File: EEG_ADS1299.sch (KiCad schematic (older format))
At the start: 76 parts, among them IC1 ADS1299, P1 CONN_2, P2 CONN_2, P3 CONN_01X08, U1 TPS2294x, U2 TPS61222, U3 NRF528XX-QFAA, U4 MPU-9250, U5 INA828, U6 INA828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

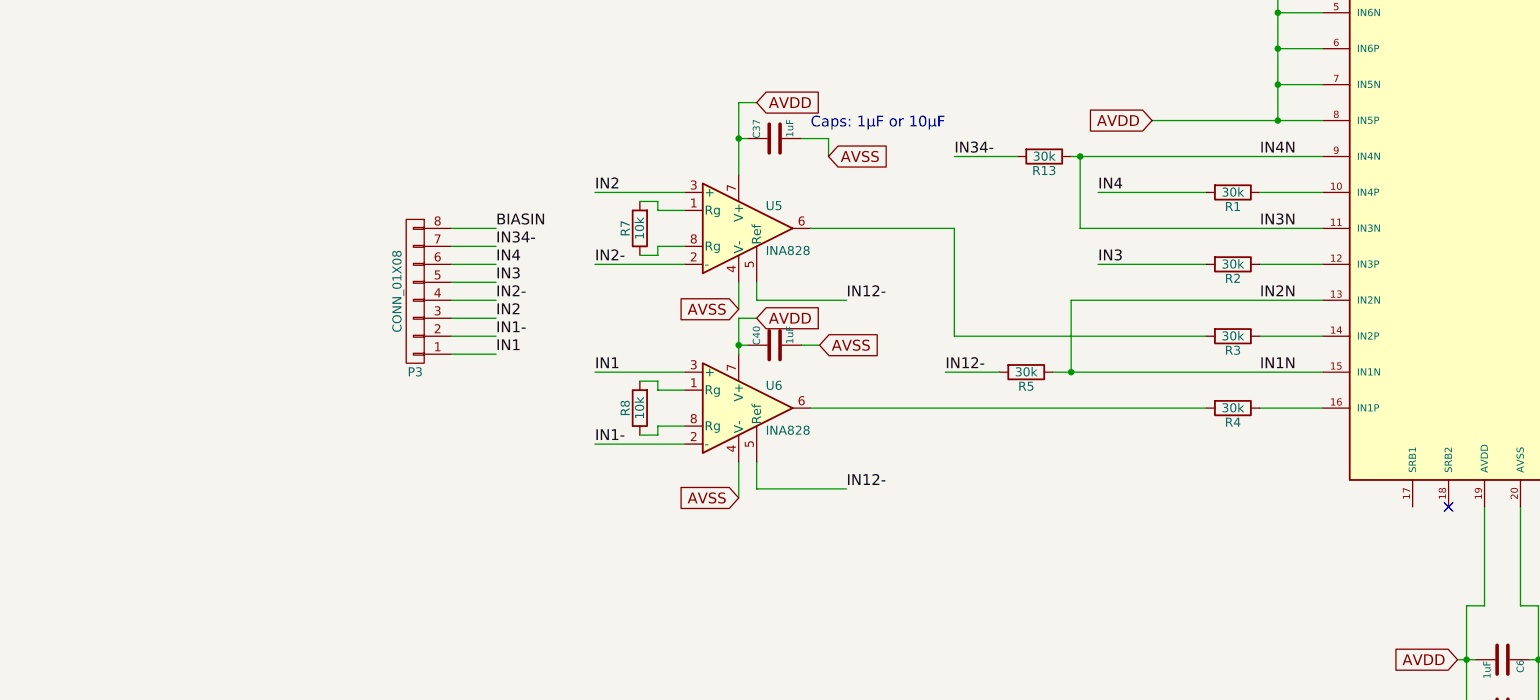
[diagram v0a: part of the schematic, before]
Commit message: Updated schematic and pcb design to reflect final EEG design: Connected SRB1 to IN12-.
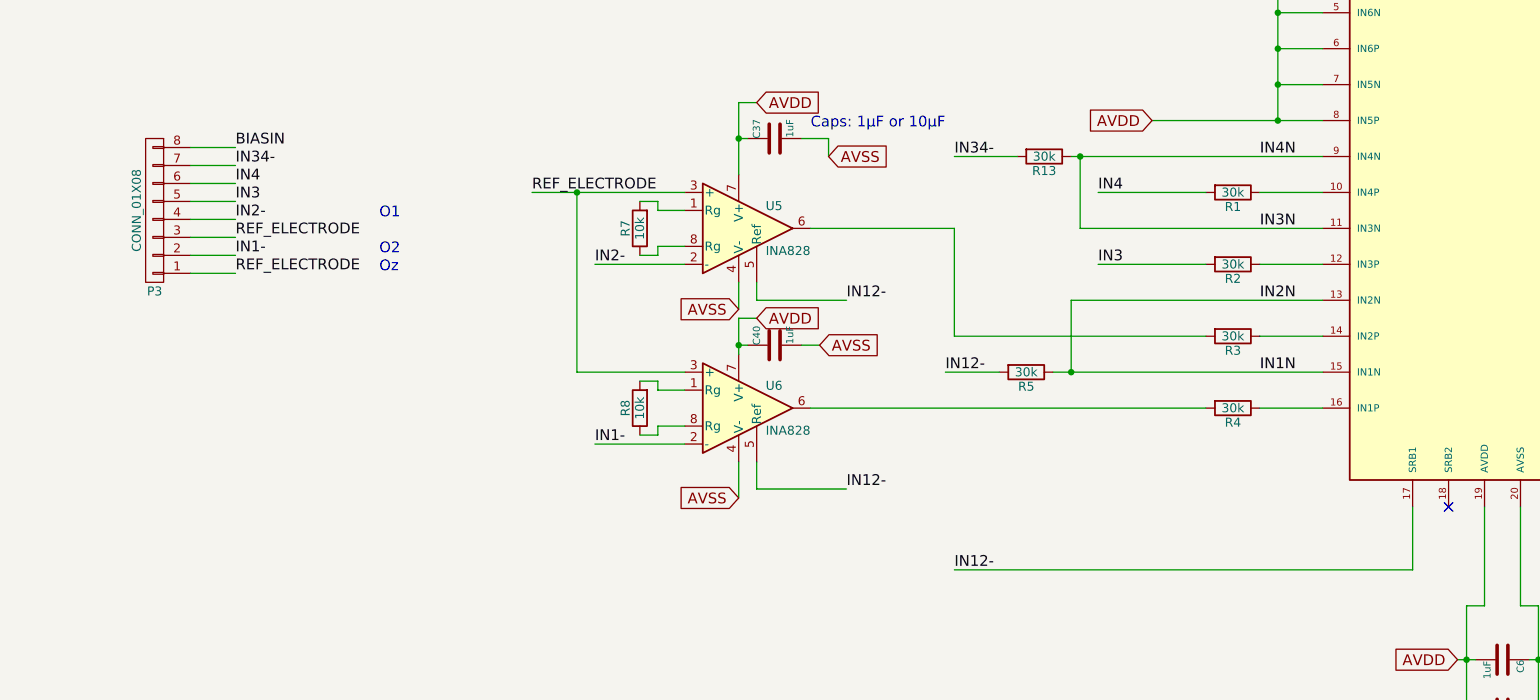
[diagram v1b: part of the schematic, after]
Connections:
- net IN2 is gone; now on net REF_ELECTRODE: P3.3 (P3), U5.3 (+)
- net IN12-: now also IC1.17 (SRB1)
- net IN1 renamed REF_ELECTRODE
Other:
- note added: "O1"
- note added: "O2"
- note added: "Oz"
- moved on the sheet: P3
